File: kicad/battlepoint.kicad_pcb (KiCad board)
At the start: 2 copper layers, 101.6 x 154.9 mm, 20 parts, among them J1 BTNS, J2 TMR_LEDS, J3 CAP_LEDS, P13 BTNS_IN, P14 OLED_OUT, P17 BTNS_OUT, P5 SPK, P8 AUDIO_JACK, SW1 BTN_UP, SW2 BTN_DWN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

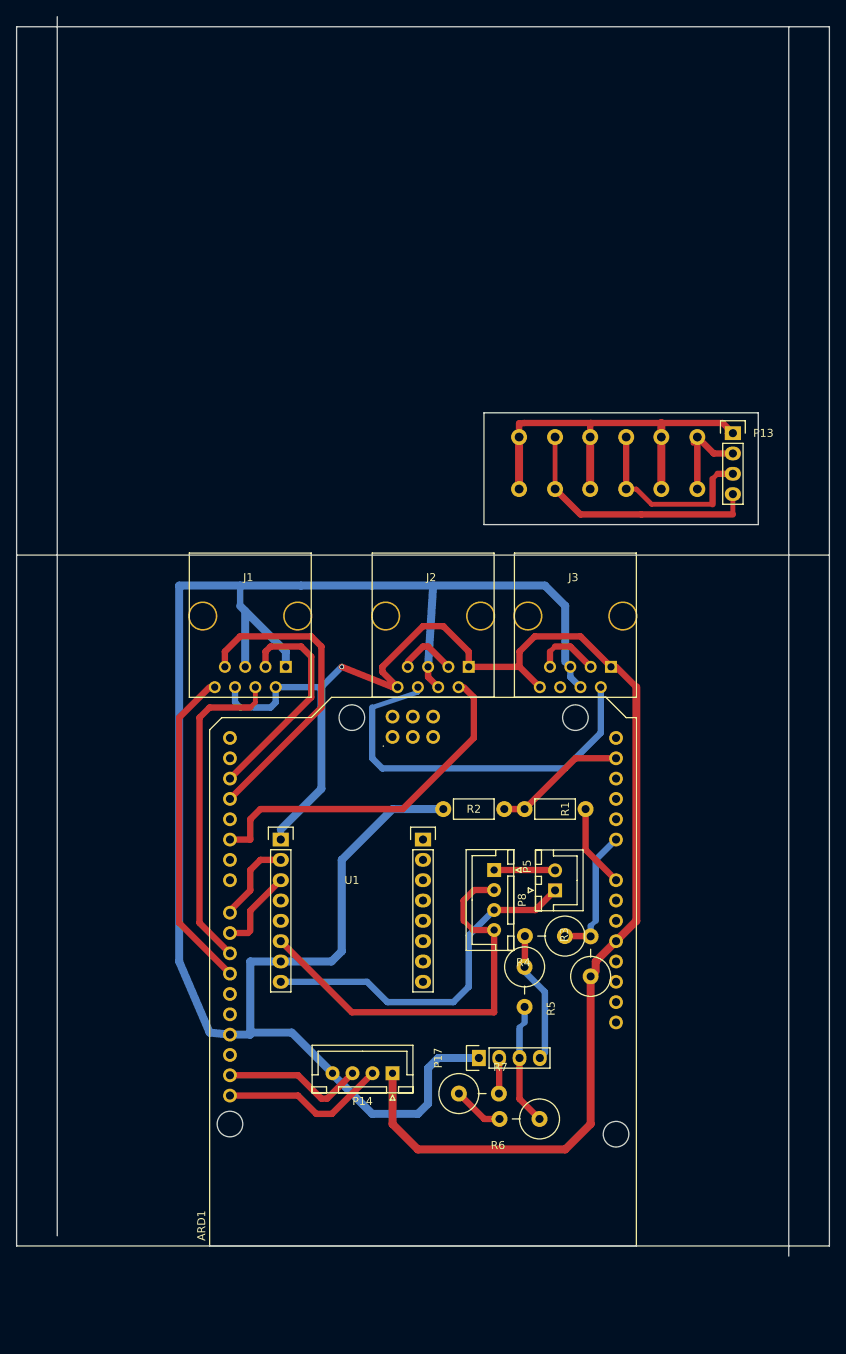
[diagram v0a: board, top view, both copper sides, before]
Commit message: base version without regulator
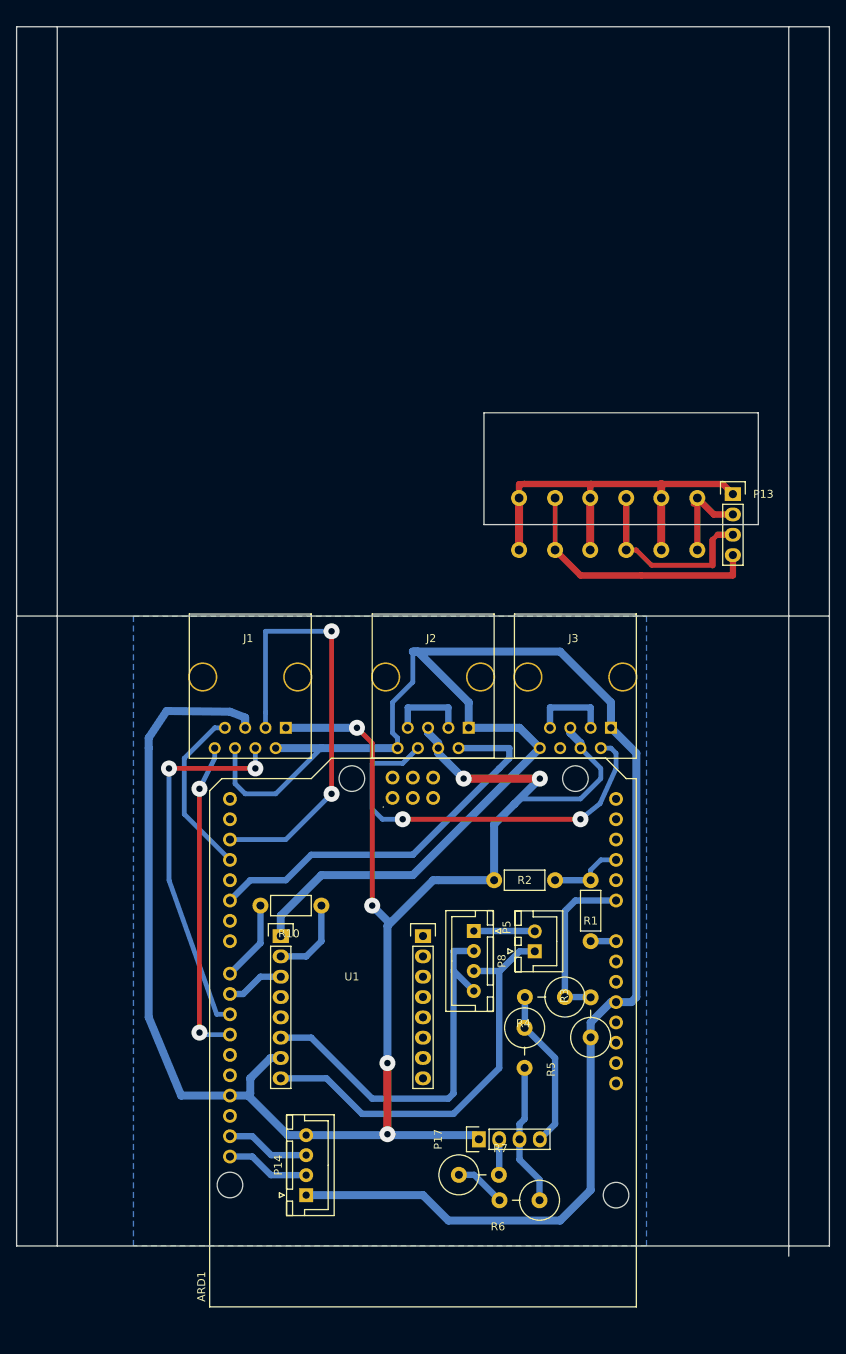
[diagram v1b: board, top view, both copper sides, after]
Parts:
- added R10: 1K, Resistors_ThroughHole:Resistor_Horizontal_RM7mm, F.Cu at (57.1, 151.8)
- moved P14 18.7 mm to (55.2, 188.0), turned to 90 degrees
- moved R1 16.5 mm to (90.8, 156.2), turned to 90 degrees
- moved U1 12.1 mm to (50.8, 155.6)
- moved R2 10.9 mm to (86.4, 148.6)
- moved P17 10.2 mm to (76.8, 181.0)
- moved R6 10.2 mm to (81.9, 188.6)
- moved R7 10.2 mm to (76.8, 185.4)
- moved P8 8.03 mm to (76.2, 154.9)
- moved P5 8.03 mm to (83.8, 157.5)
- moved ARD1 7.62 mm to (96.5, 201.9)
- moved J1 7.62 mm to (48.3, 123.2)
- moved J2 7.62 mm to (71.1, 123.2)
- moved J3 7.62 mm to (88.9, 123.2)
- moved P13 7.62 mm to (108.6, 100.3)
- moved R3 7.62 mm to (90.8, 165.7)
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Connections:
- ARD1 pad A2: Net-(ARD1-PadA2) -> A2
- ARD1 pad A4: A4 -> Net-(ARD1-PadA4)
- R1 pad 2: A4 -> A2
- R2 pad 1: A4 -> A2
- U1 pad 2: D8 -> Net-(R10-Pad1)
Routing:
- net +5V: track 187.4 -> 245.7 mm, vias 1 -> 0
- net D2: track 27.9 -> 55.7 mm, vias 0 -> 2
- net D3: track 39.1 -> 21.7 mm
- net A4: track 16.6 -> 0.00 mm
- net GND: track 305.4 -> 292.7 mm, vias 0 -> 6
- net SCL: track 21.2 -> 10.5 mm
- net Net-(R10-Pad1): track 0.00 -> 10.3 mm
- net A2: track 0.00 -> 9.42 mm
- net SDA: track 18.1 -> 10.5 mm
- net Net-(P5-Pad1): track 44.9 -> 52.3 mm
- net Net-(ARD1-PadVIN): track 10.5 -> 3.17 mm
- net D10: track 41.1 -> 46.8 mm, vias 0 -> 2
- net D5: track 44.7 -> 49.9 mm
- net A0: track 16.6 -> 20.9 mm
- net Net-(P17-Pad4): track 16.6 -> 20.2 mm
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- added copper zone on B.Cu, net GND
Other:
- board size 101.6 x 154.9 mm -> 101.6 x 153.7 mm
- net class BIG added: clearance 0.3, trace_width 1, via_dia 2, via_drill 0.8
- net class Default: trace_width 0.8 -> 0.6; via_dia 0.6 -> 2; via_drill 0.4 -> 0.8
- net class PWR: via_dia 0.6 -> 2; via_drill 0.4 -> 0.8
- net class SMALL: via_dia 0.6 -> 2; via_drill 0.4 -> 0.8
- board text added: "GND"
- board text added: "J6"

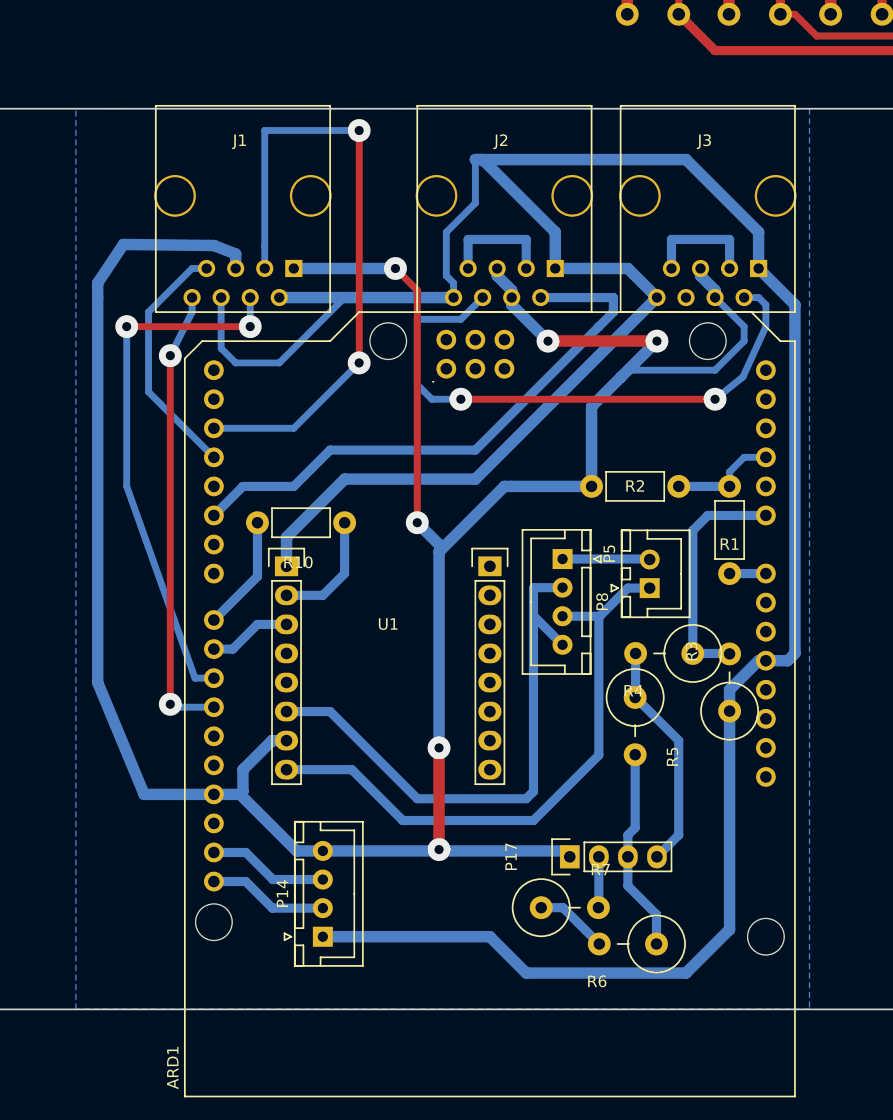
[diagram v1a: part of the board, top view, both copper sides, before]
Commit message: add regulator circuit
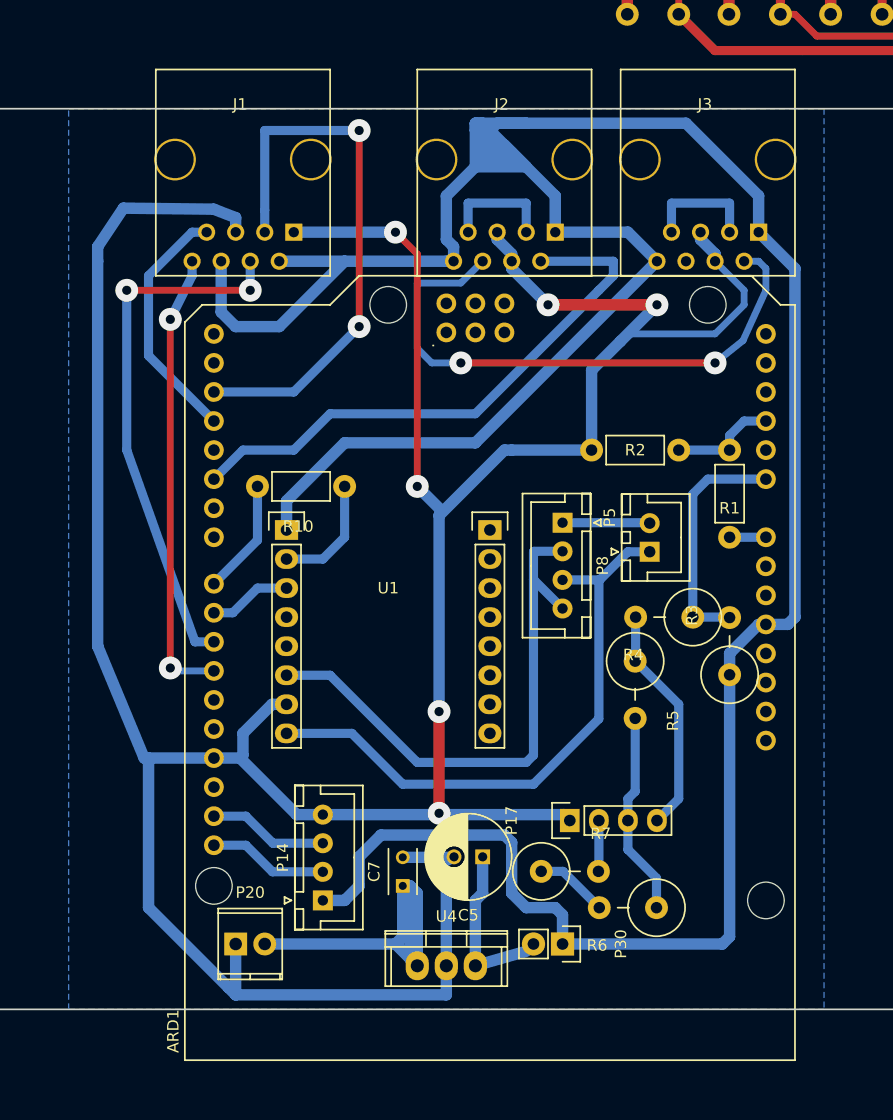
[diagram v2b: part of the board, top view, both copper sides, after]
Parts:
- added C5: 22uf, Capacitors_ThroughHole:C_Radial_D7.5_L11.2_P2.5, F.Cu at (69.2, 181.0)
- added C7: 0.1uf, Capacitors_ThroughHole:C_Rect_L4_W2.5_P2.5, F.Cu at (62.2, 183.5)
- added P20: AUX_PWR, Terminal_Blocks:TerminalBlock_Pheonix_MPT-2.54mm_2pol, F.Cu at (47.6, 188.6)
- added P30: EXT_PWR_JP, Pin_Headers:Pin_Header_Straight_1x02, F.Cu at (76.2, 188.6)
- added U4: L4940, Power_Integrations:TO-220, F.Cu at (66.0, 190.5)
- moved ARD1 3.18 mm to (96.5, 198.8)
- moved P14 3.18 mm to (55.2, 184.8)
- moved P8 3.18 mm to (76.2, 151.8)
- moved R1 3.18 mm to (90.8, 153.0)
- moved R2 3.18 mm to (86.4, 145.4)
- moved R3 3.18 mm to (90.8, 162.6)
- moved R6 3.18 mm to (81.9, 185.4)
- moved J1 3.17 mm to (48.3, 120.0)
- moved J2 3.17 mm to (71.1, 120.0)
- moved J3 3.17 mm to (88.9, 120.0)
- moved P17 3.17 mm to (76.8, 177.8)
- moved P5 3.17 mm to (83.8, 154.3)
- moved R10 3.17 mm to (57.1, 148.6)
- moved R4 3.17 mm to (85.1, 160.0)
- moved R5 3.17 mm to (82.5, 166.4)
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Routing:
- net GND: track 292.7 -> 357.1 mm
- net +5V: track 245.7 -> 282.9 mm
- net Net-(C7-Pad1): track 0.00 -> 35.9 mm
- net Net-(C5-Pad1): track 0.00 -> 15.3 mm
- net D2: track 55.7 -> 49.4 mm
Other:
- net class Default: trace_width 0.6 -> 0.8

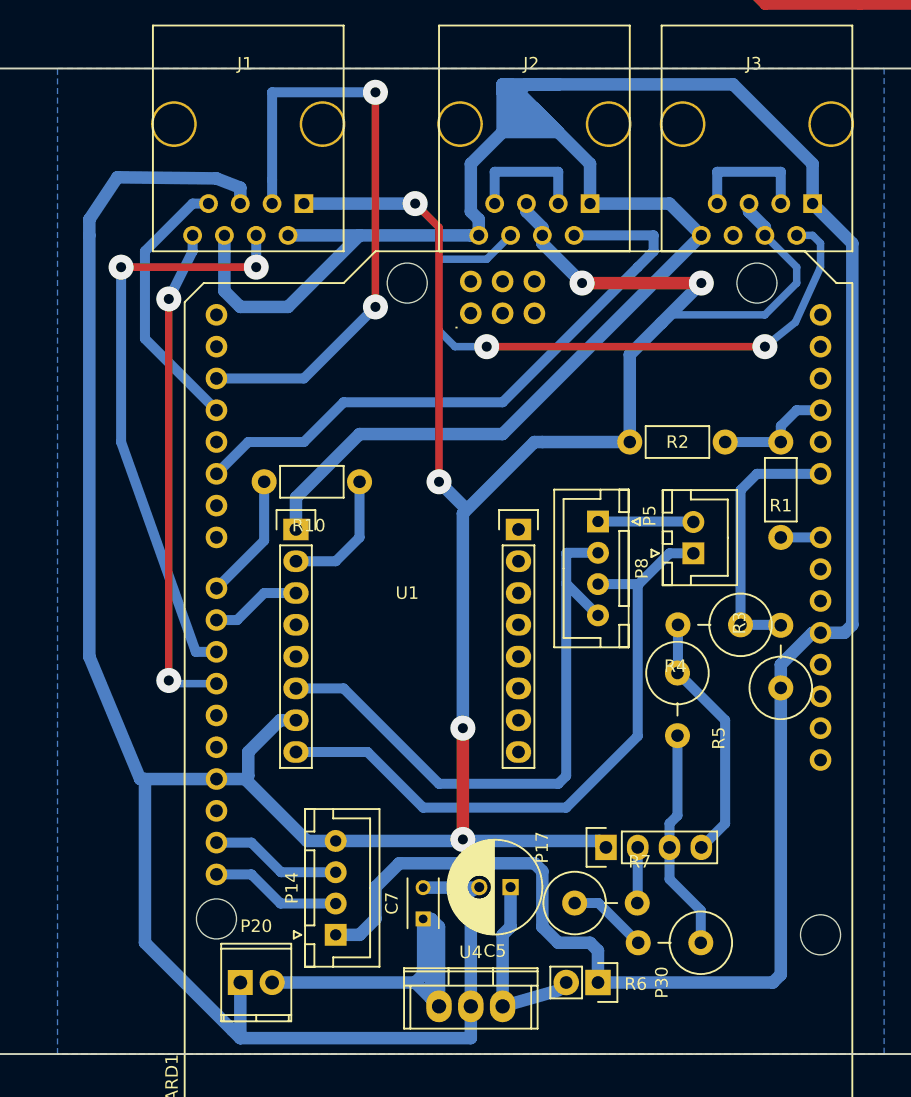
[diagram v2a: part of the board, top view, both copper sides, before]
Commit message: made the pads bigger
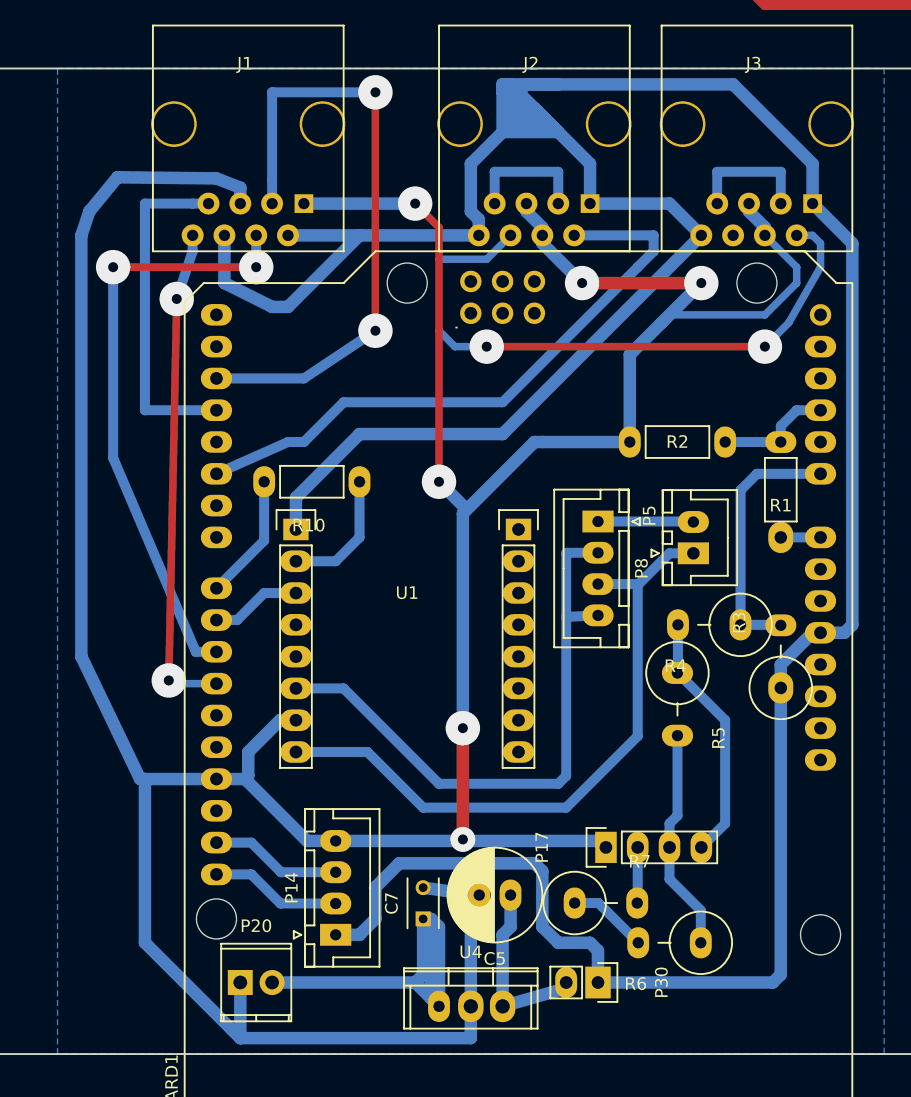
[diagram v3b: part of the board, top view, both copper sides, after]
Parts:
- moved C5 0.64 mm to (69.2, 181.6)
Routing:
- net D3: track 21.7 -> 27.3 mm
- net Net-(P8-Pad2): track 48.9 -> 47.9 mm
- net D10: track 46.8 -> 47.7 mm
- net +5V: track 282.9 -> 282.2 mm
- net D2: track 49.4 -> 50.0 mm
- net Net-(C5-Pad1): track 15.3 -> 14.7 mm
- net D5: track 49.9 -> 49.4 mm
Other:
- net class BIG: via_dia 2 -> 2.75
- net class Default: via_dia 2 -> 2.75
- net class PWR: via_dia 2 -> 2.75
- net class SMALL: via_dia 2 -> 2.75

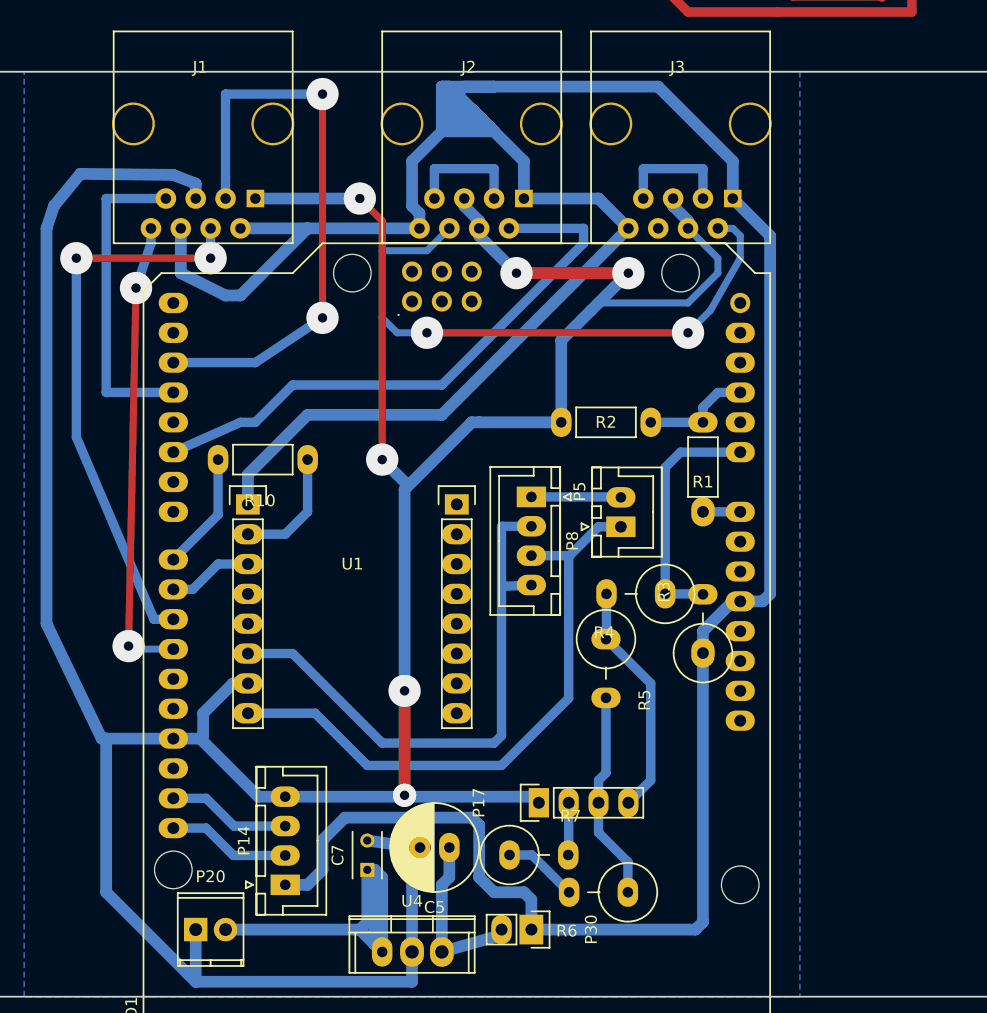
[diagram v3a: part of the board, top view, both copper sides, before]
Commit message: reversed the top layer
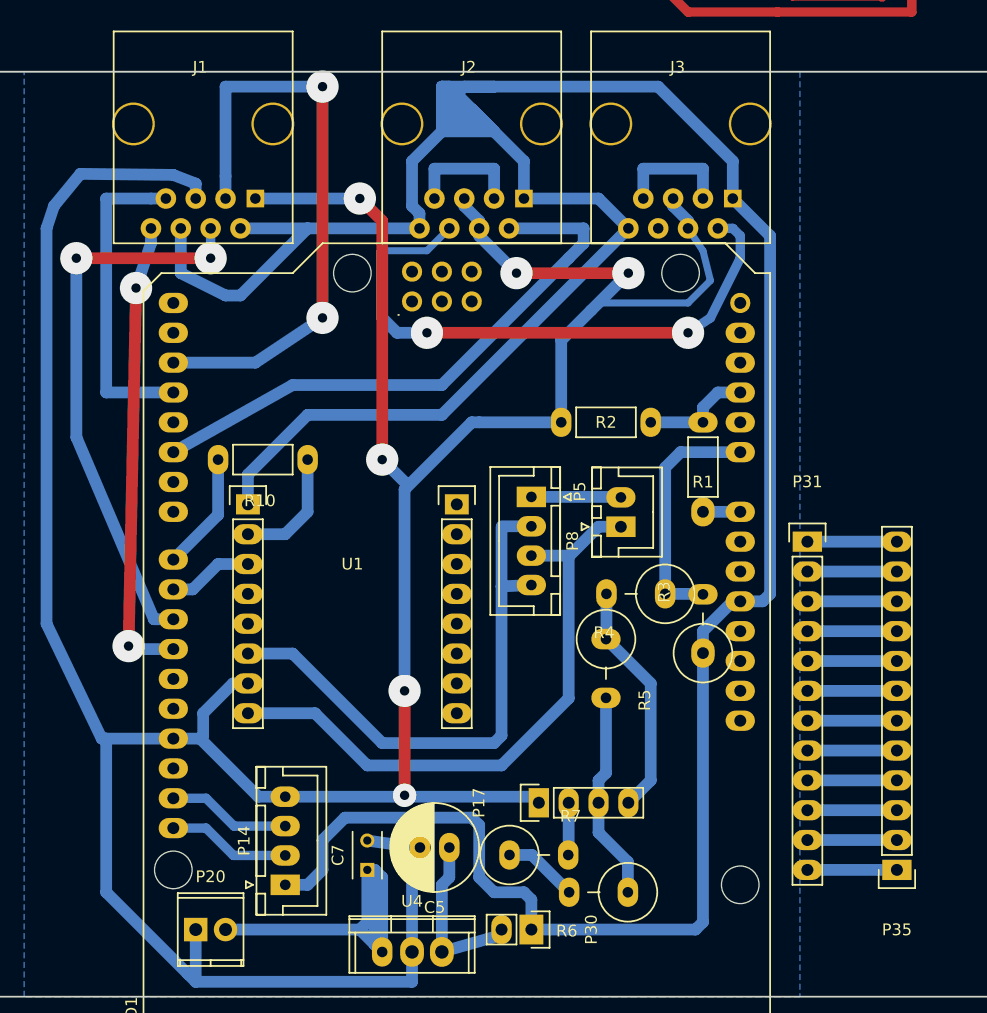
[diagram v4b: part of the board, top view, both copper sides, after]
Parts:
- added P31: CONN_01X12, Pin_Headers:Pin_Header_Straight_1x12, F.Cu at (99.7, 155.6)
- added P35: CONN_01X12, Pin_Headers:Pin_Header_Straight_1x12, F.Cu at (107.3, 183.5)
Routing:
- net Net-(P31-Pad9): track 0.00 -> 7.62 mm
- net Net-(P31-Pad8): track 0.00 -> 7.62 mm
- net Net-(P31-Pad7): track 0.00 -> 7.62 mm
- net Net-(P31-Pad6): track 0.00 -> 7.62 mm
- net Net-(P31-Pad5): track 0.00 -> 7.62 mm
- net Net-(P31-Pad4): track 0.00 -> 7.62 mm
- net Net-(P31-Pad3): track 0.00 -> 7.62 mm
- net Net-(P31-Pad2): track 0.00 -> 7.62 mm
- net Net-(P31-Pad12): track 0.00 -> 7.62 mm
- net Net-(P31-Pad11): track 0.00 -> 7.62 mm
- net Net-(P31-Pad10): track 0.00 -> 7.62 mm
- net Net-(P31-Pad1): track 0.00 -> 7.62 mm
- net D2: track 50.0 -> 51.3 mm
- net GND: track 357.5 -> 356.6 mm
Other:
- net class Default: trace_width 0.8 -> 1
- board text added: "BATTLEPOINT v1.1"
